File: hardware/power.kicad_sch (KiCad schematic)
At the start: 36 parts, among them Q4 DMN1150UFB-7B, U3 TI LMR51430YFDDCR, U4 TI LMR51430YFDDCR, U5 TPS2116DRLR, U6 NCV8187AMT180TAG, U7 LP5912-3.3DRVR

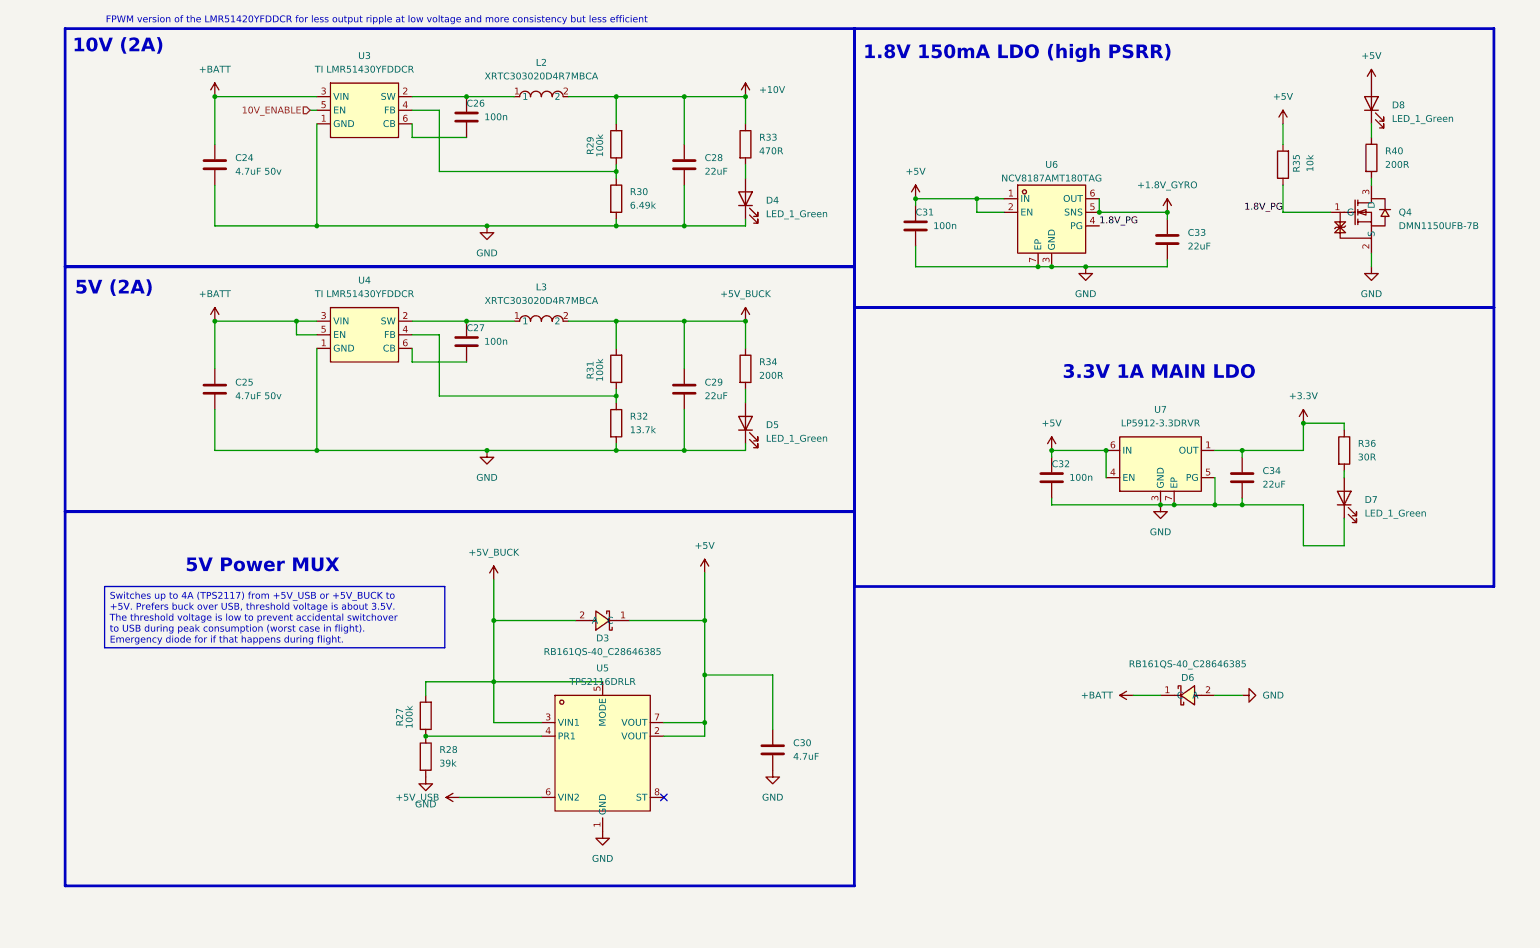
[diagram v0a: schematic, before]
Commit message: Rev 2 (RP2354A): finalize design, update docs, clean repo (#5)
* docs(readme): add analog OSD BOM to Rev 2 change list

Document OSD debugging findings and component changes as a new
Analog OSD section in the Rev 2 Change List:
- HW-12: U19 op-amp TLV9061IDPWR -> COS8051SOT (175MHz video-grade RRIO)
- HW-13: output front-end add AC-couple + DC-restore, power U19 from +5V
- HW-14: U20 comparator TLV3201AIDBVR -> TLV7031DPWR (push-pull, X2SON, ~75% smaller)
- HW-15: add OSD_EN select pull-down (datasheet-required, defaults to pass-through)
- U18 / D9 verified correct, no change; OSD GPIO mapping noted (PA4/5/6)

Also fix HW-11 beeper GPIO: GPIO6 -> GPIO7 (GPIO6 is OSD_SYNC per netlist).

Co-Authored-By: Claude Opus 4.8 (1M context) <noreply@anthropic.com>

* many tiny improvements

- I/O correctness
- SPI0/SPI1/I2C0 bus corrections
- decoupling of DVDD
- ADC_AVDD as per RPi documents
- removal of SBUS
- connect ESC serial
- remove RUN RC-circuit as per RPi documentation
- some more cleanup for readability
- gyro CLKIN decision
- I2C 4.7k pullup

* RP2354A

* piu1

* switch spi

* Update OpenFC.kicad_pcb

* routex2

* some minor tweaks

- remove some unnecessary resistors
- slightly higher 10V rail to account for voltage drop
- some cleanup
- simpler PG 1.8V circuit

* Update imu.kicad_sch

* LED resistors

Also reduced the amount of different resistors for cheaper assembly

* Delete leds.kicad_sch

* remove some unneeded decoupling caps from RP2350

* update MOSFET part numbers

* OSD

* ROUTE

* clean libs

* details

* led names

* Clean routing

* docs: rewrite README + CLAUDE.md for finalized Rev 2 (RP2354A)

Rev 2 is a substantial redesign that the docs no longer matched. Updated
both to the actual schematic, verified from the current netlist:

- MCU: RP2354B (QFN-80, GPIO0-47) -> RP2354A (QFN-60, GPIO0-29). Full GPIO
  map re-derived from the netlist + QFN-60 pinout; all 30 GPIO documented.
- IMU moved to SPI1, microSD to SPI0; ref designators re-annotated
  (op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
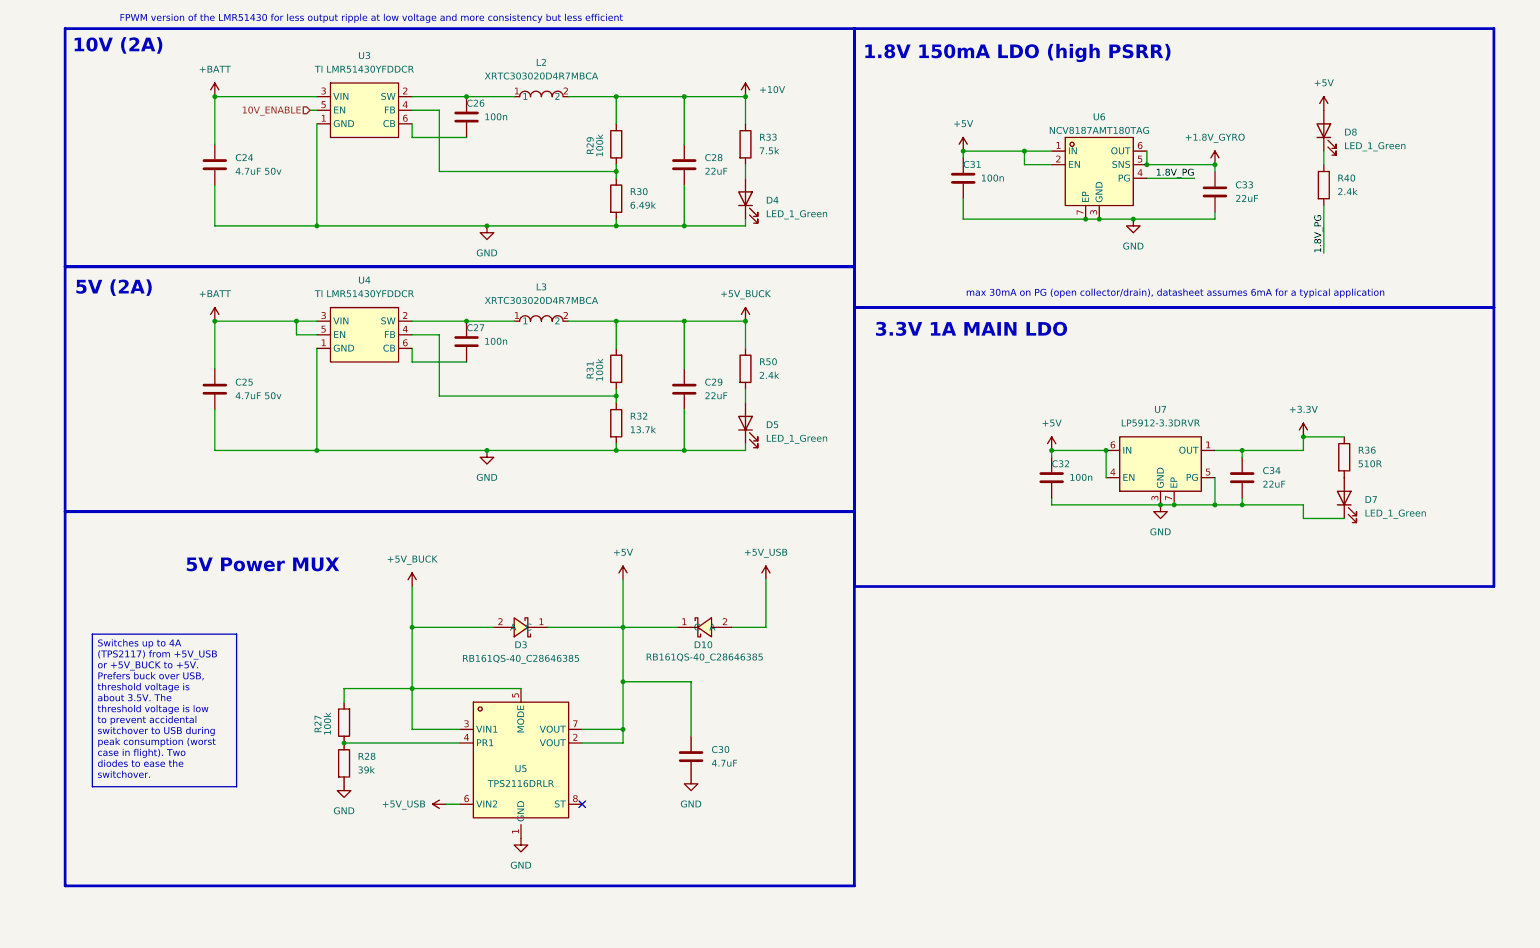
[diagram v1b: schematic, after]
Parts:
- removed D6: RB161QS-40_C28646385, lib:SOD-882_L1.0-W0.6-RD, symbol lib:RB161QS-40_C28646385
- removed Q4: DMN1150UFB-7B, lib:DFN-3L_L1.0-W0.6-P0.65-BR, symbol lib:DMN1150UFB-7B
- removed R34: 200R, Resistor_SMD:R_0201_0603Metric, symbol Device:R
- removed R35: 10k, Resistor_SMD:R_0201_0603Metric, symbol Device:R
- added D10: RB161QS-40_C28646385, lib:SOD-882_L1.0-W0.6-RD, symbol lib:RB161QS-40_C28646385
- added R50: 2.4k, Resistor_SMD:R_0201_0603Metric, symbol Device:R
- R30: LCSC C474786 -> C2107920; MPN RC0201FR-076K8L -> (none); Manufacturer YAGEO -> (none)
- R33: value 470R -> 7.5k; LCSC C473464 -> C474437; MPN 0201WMF4700TEE -> (none); Manufacturer UNI-ROYAL -> (none)
- R36: value 30R -> 510R; LCSC C778391 -> C57784; MPN NQ01WMJ0300TEE -> (none); Manufacturer UNI-ROYAL -> (none)
- R40: value 200R -> 2.4k; LCSC C270359 -> C166281; MPN 0201WMF2000TEE -> (none); Manufacturer UNI-ROYAL -> (none)
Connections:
- net +5V: now also D10.1 (C)
- net +5V_BUCK: now also R50.1
- net +5V_USB: now also D10.2 (A)
- net 1.8V_PG: now also R40.2
- net at D5.2 (A): now also R50.2
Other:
- note added: "FPWM version of the LMR51430 for less output ripple at low voltage and more consistency but less efficient"
- note added: "max 30mA on PG (open collector/drain), datasheet assumes 6mA for a typical application"
- note removed: "FPWM version of the LMR51420YFDDCR for less output ripple at low voltage and more consistency but less efficient"
- moved on the sheet: C30, C31, C33, D3, D8, R27, R28, R36, R40, U5, U6

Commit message: docs(schematic): add design annotations to all sheets
Port on-canvas engineering comments from OpenFC-Lite (RP2354B), adapted to the
Mini layout. +41 text items across root, rp2350a, power, imu, osd, blackbox,
pads. Annotation/text only — no net or connectivity changes. Mirrors
hardware/DESIGN_NOTES.md.

Co-Authored-By: Claude Opus 4.8 (1M context) <noreply@anthropic.com>
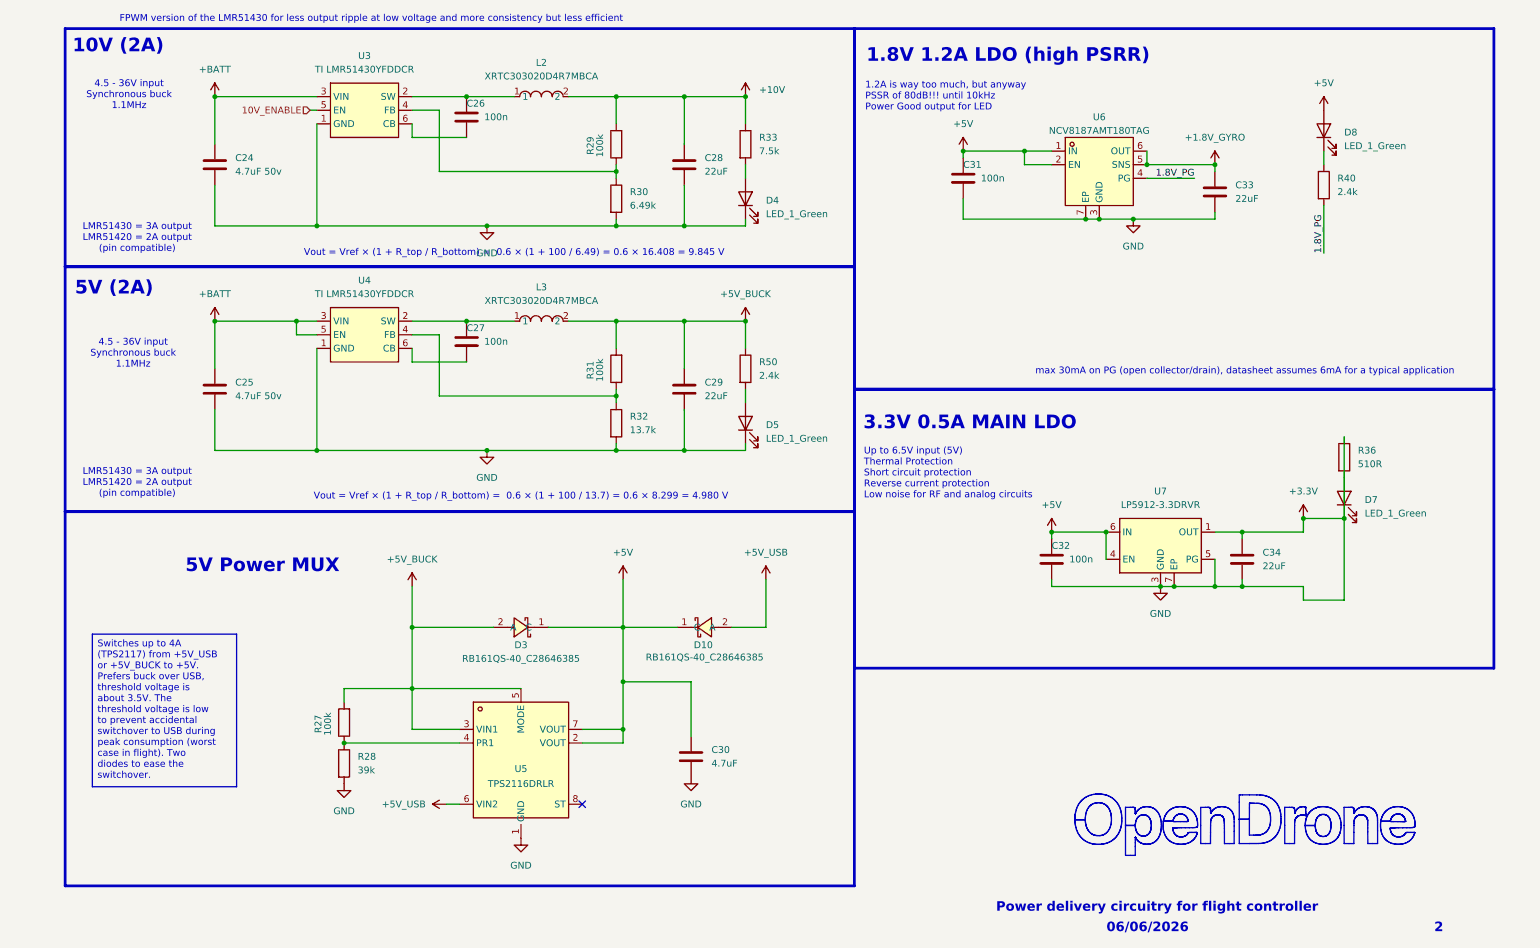
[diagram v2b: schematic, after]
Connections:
- net GND is gone; now on net +3.3V: C24.2, C25.2, C28.2, C29.2, C30.2, C31.2, C32.2, C33.2, C34.2, D4.1 (K), D5.1 (K), D7.1 (K), R28.2, R30.2, R32.2, U3.1 (GND), U4.1 (GND), U5.1 (GND), U6.3 (GND), U6.7 (EP), U7.3 (GND), U7.5 (PG), U7.7 (EP)
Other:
- note added: "06/06/2026"
- note added: "1.2A is way too much, but anyway PSSR of 80dB!!! until 10kHz Power Good output for LED"
- note added: "1.8V 1.2A LDO (high PSRR)"
- note added: "2"
- note added: "3.3V 0.5A MAIN LDO"
- note added: "4.5 - 36V input Synchronous buck 1.1MHz"
- note added: "LMR51430 = 3A output LMR51420 = 2A output (pin compatible)"
- note added: "Power delivery circuitry for flight controller"
- note added: "Up to 6.5V input (5V) Thermal Protection Short circuit protection Reverse current protection Low noise for RF and analog circuits"
- note added: "Vout = Vref × (1 + R_top / R_bottom) = 0.6 × (1 + 100 / 13.7) = 0.6 × 8.299 = 4.980 V"
- note added: "Vout = Vref × (1 + R_top / R_bottom) = 0.6 × (1 + 100 / 6.49) = 0.6 × 16.408 = 9.845 V"
- note removed: "1.8V 150mA LDO (high PSRR)"
- note removed: "3.3V 1A MAIN LDO"
- moved on the sheet: C32, C34, U7

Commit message: chore(bom): consolidate LCSC Part -> LCSC field across schematic, library, footprints, project
Single canonical LCSC field (was split LCSC / LCSC Part). Every part resolves to one LCSC code; netlist verified, no duplicates. Includes Rev2 re-annotation resync re-save.

Co-Authored-By: Claude Opus 4.8 (1M context) <noreply@anthropic.com>
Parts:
- D10, D3: LCSC (none) -> C28646385; LCSC Part C28646385 -> (none)
- L2, L3: LCSC (none) -> C39846837; LCSC Part C39846837 -> (none)
- U3, U4: LCSC (none) -> C5219261; LCSC Part C5219261 -> (none)
- U5: LCSC (none) -> C3235557; LCSC Part C3235557 -> (none)
- U6: LCSC (none) -> C893189; LCSC Part C893189 -> (none)
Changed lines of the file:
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@@
 			)
 		)
-		(property "LCSC Part" "C28646385"
+		(property "LCSC" "C28646385"
 			(at 133.35 147.32 0)
 			(hide yes)
@@
 			)
 		)
-		(property "LCSC Part" "C39846837"
+		(property "LCSC" "C39846837"
 			(at 102.87 48.26 0)
 			(hide yes)
@@
 			)
 		)
-		(property "LCSC Part" "C5219261"
+		(property "LCSC" "C5219261"
 			(at 69.85 95.25 0)
 			(hide yes)
@@
 			)
 		)
-		(property "LCSC Part" "C893189"
+		(property "LCSC" "C893189"
 			(at 207.01 66.04 0)
 			(hide yes)
@@
 			)
 		)
-		(property "LCSC Part" "C3235557"
+		(property "LCSC" "C3235557"
 			(at 99.06 171.45 0)
 			(hide yes)
@@
 			)
 		)
-		(property "LCSC Part" "C39846837"
+		(property "LCSC" "C39846837"
 			(at 102.87 90.17 0)
 			(hide yes)
@@
 			)
 		)
-		(property "LCSC Part" "C28646385"
+		(property "LCSC" "C28646385"
 			(at 99.06 127 0)
 			(hide yes)
@@
 			)
 		)
-		(property "LCSC Part" "C5219261"
+		(property "LCSC" "C5219261"
 			(at 69.85 53.34 0)
 			(hide yes)
